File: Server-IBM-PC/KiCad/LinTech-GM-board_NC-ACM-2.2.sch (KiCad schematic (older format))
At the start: 78 parts, among them Q1 12000 KHz, X7 Conn_02x03_Counter_Clockwise

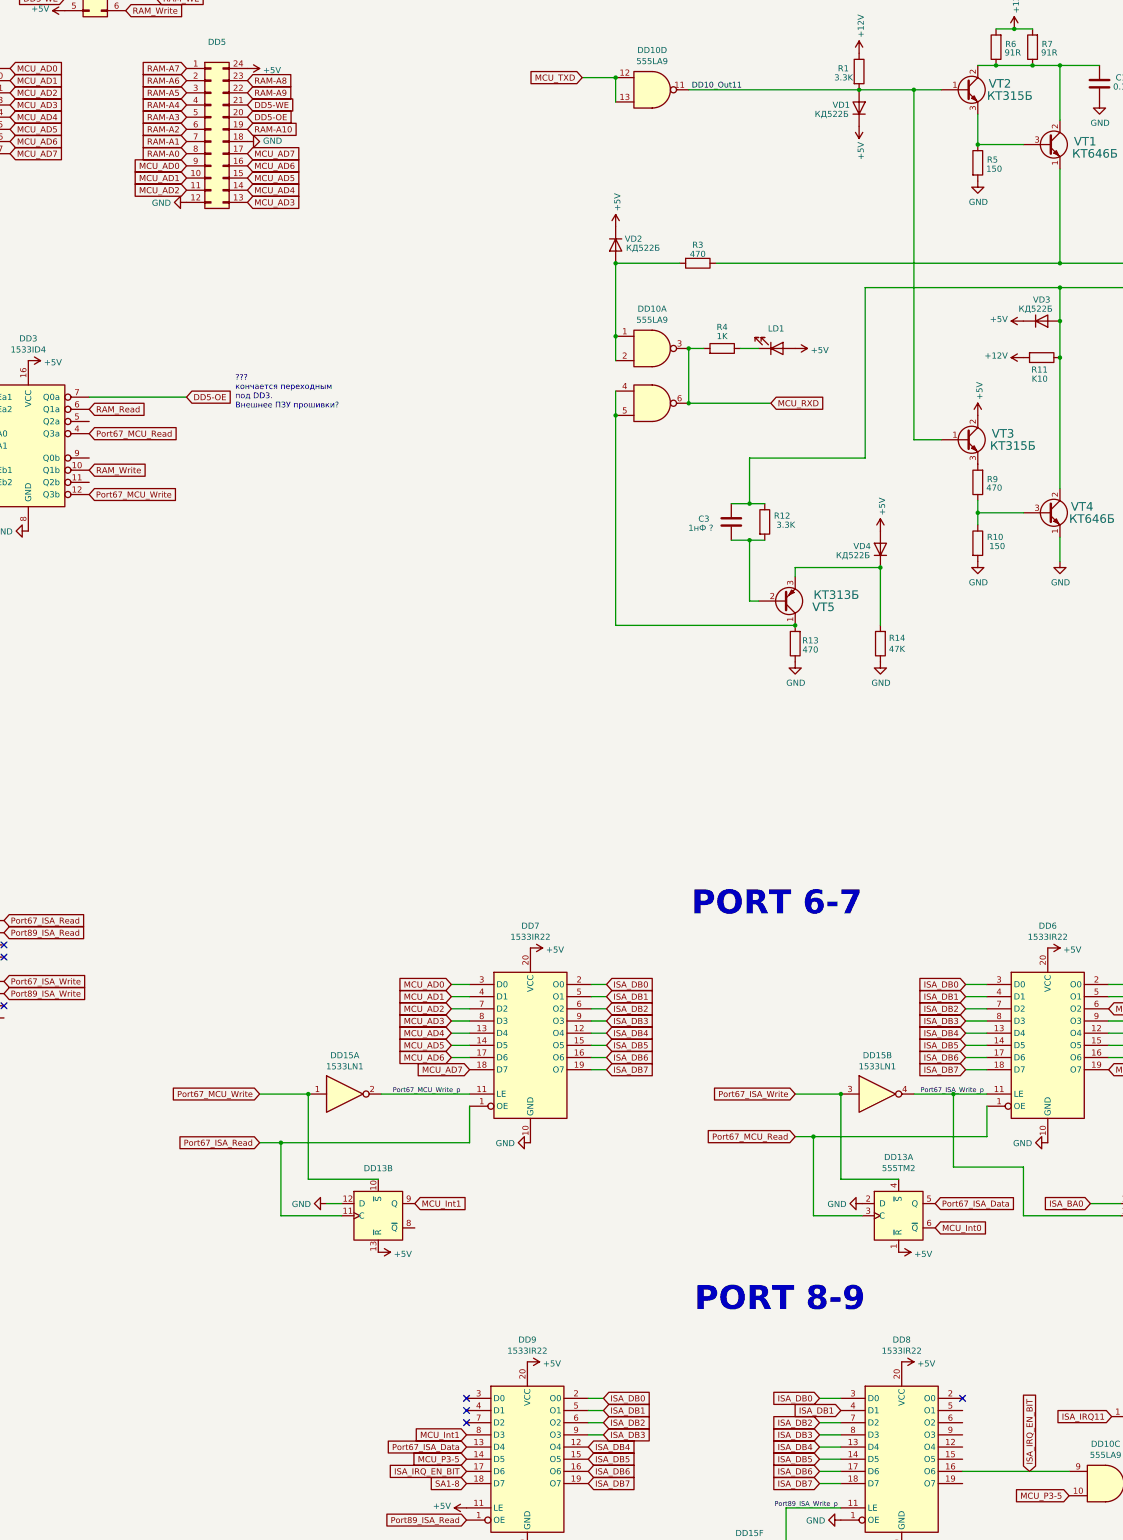
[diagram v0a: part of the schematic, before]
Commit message: FIX DD9 pin 13 wire, add R15 placeholder
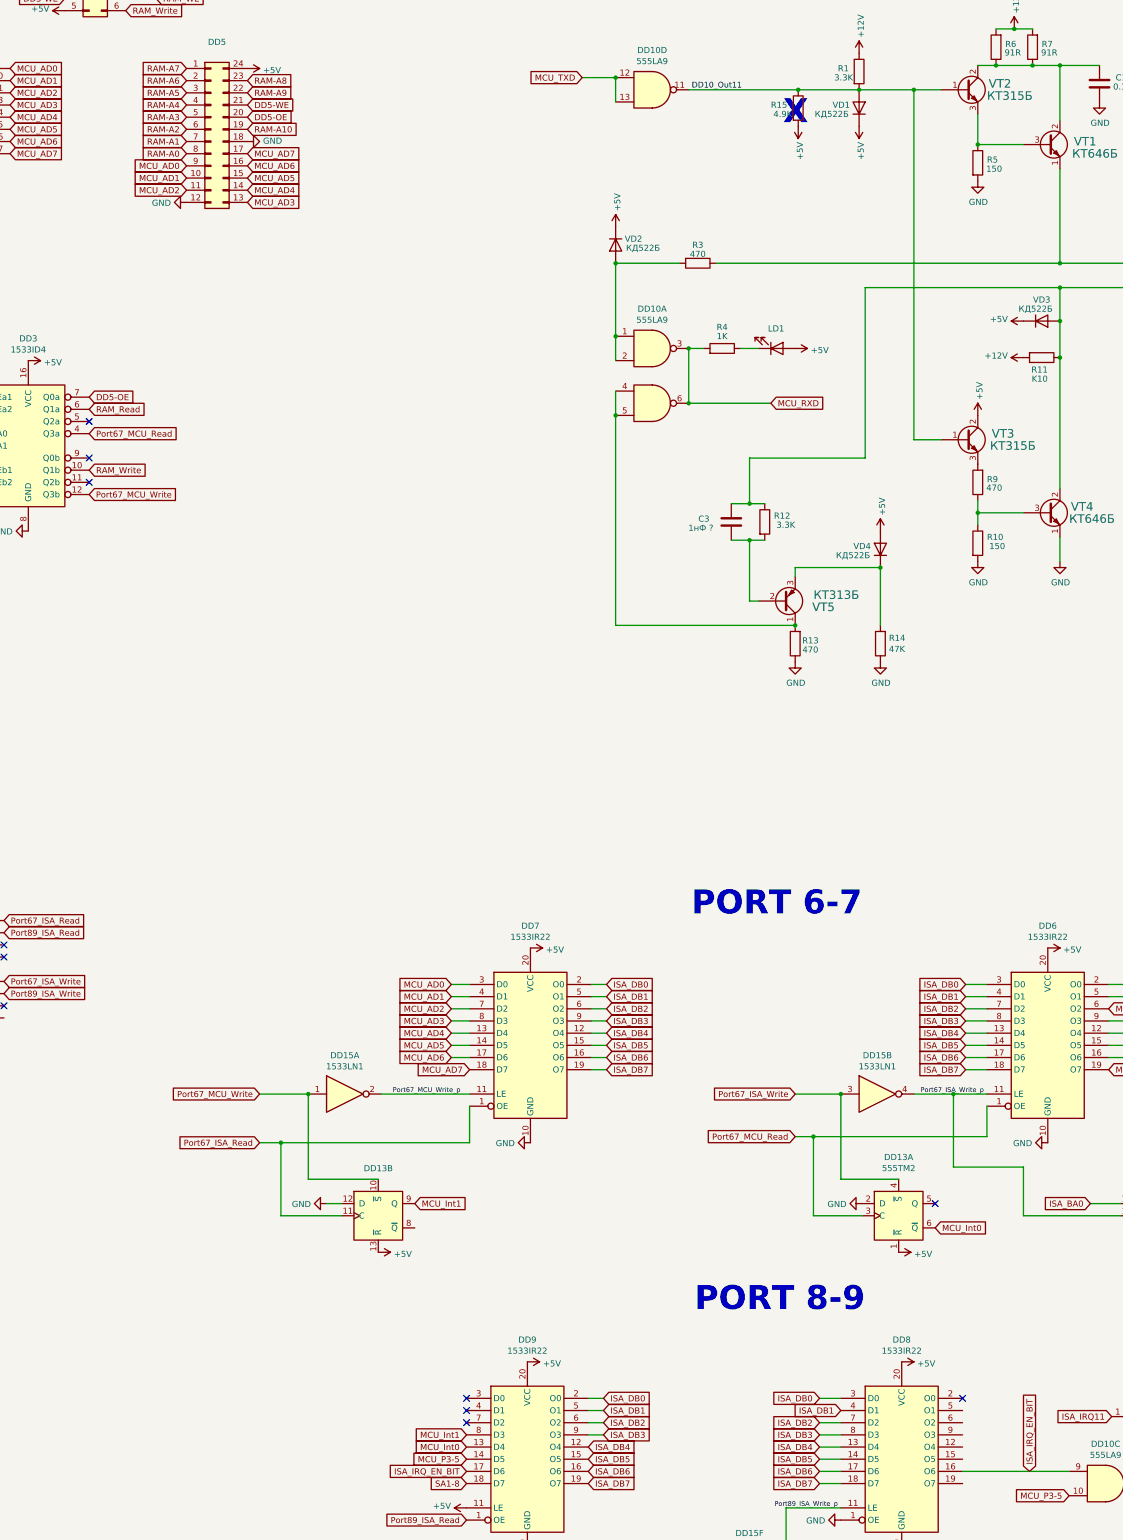
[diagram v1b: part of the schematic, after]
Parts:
- added R15: 4.9K, lib:R_Axial_DIN0309_L9.0mm_D3.2mm_P12.70mm_Horizontal, symbol Device:R
- R10, R12, R2, R9: footprint lib:R_Axial_DIN0207_L6.3mm_D2.5mm_P10.16mm_Horizontal -> lib:R_Axial_DIN0309_L9.0mm_D3.2mm_P12.70mm_Horizontal
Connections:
- net +5V: now also R15.2
- net DD10_Out11: now also R15.1
- net MCU_Int0: now also DD9.13 (D4)
- net Port67_ISA_Data: no longer names the net of DD13.5 (Q)
- net Port67_ISA_Data: no longer DD9.13 (D4)
- no-connect marks 9 -> 13
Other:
- note added: "X"
- note removed: "???\nкончается переходным\nпод DD3. \nВнешнее ПЗУ прошивки?"
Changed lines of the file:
@@
 Wire Wire Line
 	18500 13725 18950 13725
-Text GLabel 15875 13225 0    49   Input ~ 0
-Port67_ISA_Data
 Text GLabel 15875 13125 0    50   Input ~ 0
 MCU_Int1
@@
 Text GLabel 18575 10675 0    50   Input ~ 0
 Port67_MCU_Read
-Text GLabel 19725 11225 2    49   Input ~ 0
-Port67_ISA_Data
 Text GLabel 14175 10725 0    49   Input ~ 0
 Port67_ISA_Read
@@
 Text GLabel 3025 2700 0    49   Input ~ 0
 Port89_ISA_Write
-Text GLabel 13575 4600 2    50   Input ~ 0
+Text GLabel 12775 4600 2    50   Input ~ 0
 DD5-OE
 Text GLabel 11125 3200 0    50   Input ~ 0
@@
 F 0 "R2" H 3650 2500 50  0000 C CNN
 F 1 "1K" H 3650 2425 50  0000 C CNN
-F 2 "lib:R_Axial_DIN0207_L6.3mm_D2.5mm_P10.16mm_Horizontal" V 3705 2450 50  0001 C CNN
+F 2 "lib:R_Axial_DIN0309_L9.0mm_D3.2mm_P12.70mm_Horizontal" V 3705 2450 50  0001 C CNN
 F 3 "~" H 3775 2450 50  0001 C CNN
 	1    3775 2450
@@
 F 0 "R12" H 18400 5675 50  0000 L CNN
 F 1 "3.3K" H 18575 5600 50  0000 R CNN
-F 2 "lib:R_Axial_DIN0207_L6.3mm_D2.5mm_P10.16mm_Horizontal" V 18255 5625 50  0001 C CNN
+F 2 "lib:R_Axial_DIN0309_L9.0mm_D3.2mm_P12.70mm_Horizontal" V 18255 5625 50  0001 C CNN
 F 3 "~" H 18325 5625 50  0001 C CNN
 	1    18325 5625
@@
 F 0 "R9" H 20000 5275 50  0000 R CNN
 F 1 "470" H 20005 5345 50  0000 R CNN
-F 2 "lib:R_Axial_DIN0207_L6.3mm_D2.5mm_P10.16mm_Horizontal" V 20005 5300 50  0001 C CNN
+F 2 "lib:R_Axial_DIN0309_L9.0mm_D3.2mm_P12.70mm_Horizontal" V 20005 5300 50  0001 C CNN
 F 3 "~" H 20075 5300 50  0001 C CNN
 	1    20075 5300
@@
 F 0 "R10" H 20150 5850 50  0000 L CNN
 F 1 "150" H 20300 5775 50  0000 R CNN
-F 2 "lib:R_Axial_DIN0207_L6.3mm_D2.5mm_P10.16mm_Horizontal" V 20005 5800 50  0001 C CNN
+F 2 "lib:R_Axial_DIN0309_L9.0mm_D3.2mm_P12.70mm_Horizontal" V 20005 5800 50  0001 C CNN
 F 3 "~" H 20075 5800 50  0001 C CNN
 	1    20075 5800
@@
 Text GLabel 13075 1225 2    50   Input ~ 0
 MCU_A11
-Text Notes 13975 4700 0    47   ~ 0
-???\nкончается переходным\nпод DD3. \nВнешнее ПЗУ прошивки?
 Text Label 17725 2075 0    47   ~ 0
 DD10_Out11
@@
 	18200 5775 18325 5775
 Wire Wire Line
-	17700 2075 19100 2075
+	17700 2075 18600 2075
 Wire Wire Line
 	20075 1875 20225 1875
@@
 Wire Wire Line
 	19100 2075 19550 2075
-Wire Wire Line
-	12775 4600 13575 4600
 Connection ~ 17100 3500
 Wire Wire Line
@@
 Wire Wire Line
 	17925 3500 20750 3500
+Text GLabel 15875 13225 0    50   Input ~ 0
+MCU_Int0
+NoConn ~ 19725 11225
+$Comp
+L Device:R R15
+U 1 1 653B541F
+P 18600 2225
+F 0 "R15" H 18375 2250 50  0000 L CNN
+F 1 "4.9K" H 18550 2175 50  0000 R CNN
+F 2 "lib:R_Axial_DIN0309_L9.0mm_D3.2mm_P12.70mm_Horizontal" V 18530 2225 50  0001 C CNN
+F 3 "~" H 18600 2225 50  0001 C CNN
+	1    18600 2225
+	1    0    0    -1
+$EndComp
+Connection ~ 18600 2075
+Wire Wire Line
+	18600 2075 19100 2075
+$Comp
+L power:+5V #PWR0194
+U 1 1 653B5787
+P 18600 2375
+F 0 "#PWR0194" H 18600 2225 50  0001 C CNN
+F 1 "+5V" V 18615 2503 50  0000 L CNN
+F 2 "" H 18600 2375 50  0001 C CNN
+F 3 "" H 18600 2375 50  0001 C CNN
+	1    18600 2375
+	1    0    0    1
+$EndComp
+Text Notes 18475 2375 0    197  ~ 39
+X
+NoConn ~ 12775 4800
+NoConn ~ 12775 5100
+NoConn ~ 12775 5300
 $EndSCHEMATC
